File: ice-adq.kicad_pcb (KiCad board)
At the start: 4 copper layers, 86 x 84 mm, 48 parts, among them J1 T_Admisión, J2 T_Escape, J3 T_Aceite, J4 Sonda Lambda, J5 Sens. Inductivo, J6 Sens. Presión, J7 BATT, U1 MAX31855, U2 MAX31855, U3 MAX31855, U4 LM9044, U5 LM358, U6 MAX9924, U7 LM358, U8 hm10, U9 L7805

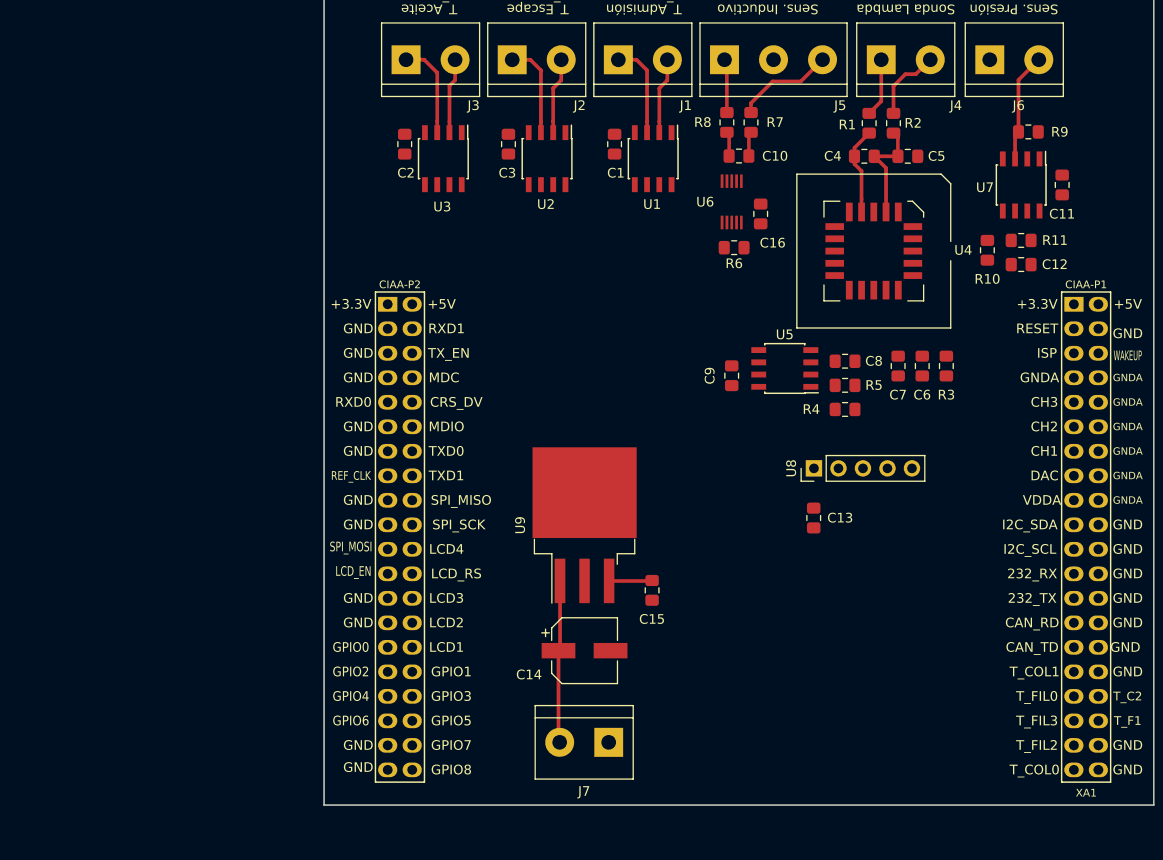
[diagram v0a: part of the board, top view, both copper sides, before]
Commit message: Se cambio pack de 7805 y de 9044
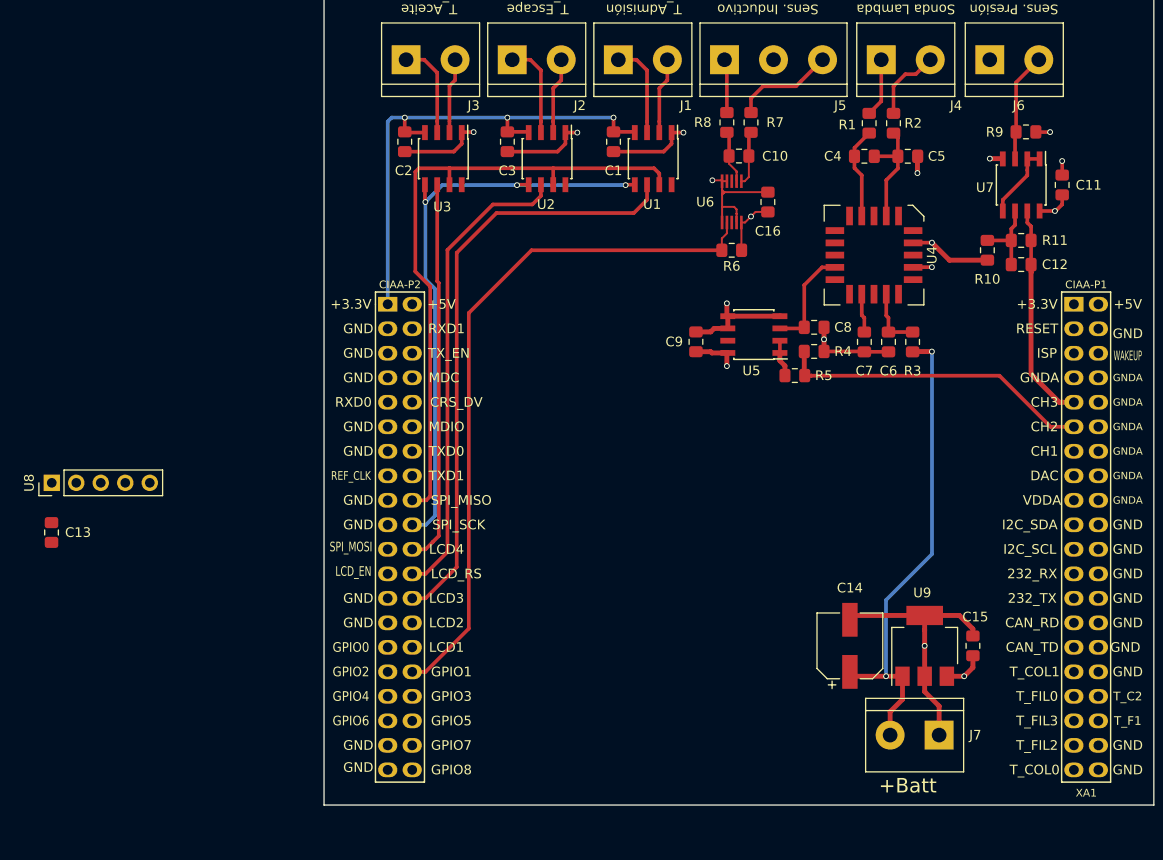
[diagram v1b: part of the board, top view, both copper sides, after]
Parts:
- U4: footprint Package_LCC:PLCC-20_SMD-Socket -> Package_LCC:PLCC-20
- U9: footprint Package_TO_SOT_SMD:TO-263-3_TabPin4 -> Package_TO_SOT_SMD:SOT-223
- moved C13 79.0 mm to (-135.2, 122.8)
- moved U8 79.0 mm to (-135.2, 117.6)
- moved U9 37.4 mm to (-44.8, 134.5)
- moved J7 34.3 mm to (-43.2, 143.8)
- moved C15 33.7 mm to (-39.8, 134.5), turned to 90 degrees
- moved C14 27.5 mm to (-52.5, 134.5), turned to 90 degrees
- moved R4 6.81 mm to (-56.2, 104.0), turned to 180 degrees
- moved R5 5.30 mm to (-58.2, 106.5)
- moved C9 5.11 mm to (-68.5, 103.0)
- moved C8 4.76 mm to (-56.2, 101.5)
- moved U5 4.76 mm to (-62.5, 102.2)
- moved C6 4.30 mm to (-48.5, 103.0)
- moved C7 4.30 mm to (-51.0, 103.0)
- moved R3 4.30 mm to (-46.0, 103.0)
- moved C16 1.44 mm to (-61.0, 88.5)
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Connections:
- C1 pad 1: Net-(C1-Pad1) -> GND
- C1 pad 2: Net-(C1-Pad2) -> +3V3
- C3 pad 1: Net-(C1-Pad1) -> GND
- C3 pad 2: Net-(C1-Pad2) -> +3V3
- U9 pad 4: GND -> (no net)
- XA1 pad 1: +3V3 -> Net-(XA1-Pad1)
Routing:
- net GND: track 0.00 -> 101.2 mm, vias 0 -> 11
- net /rpm/RPM_PULSE: track 0.00 -> 72.4 mm
- net /edu-ciaa/SO: track 0.00 -> 66.5 mm
- net /edu-ciaa/ADM_CS: track 0.00 -> 62.3 mm
- net /edu-ciaa/SCK: track 0.00 -> 61.2 mm, vias 0 -> 3
- net +3V3: track 0.00 -> 53.5 mm, vias 0 -> 3
- net /edu-ciaa/ESC_CS: track 0.00 -> 49.1 mm
- net /edu-ciaa/ACT_CS: track 0.00 -> 39.8 mm
- net +12V: track 16.8 -> 49.9 mm, vias 0 -> 2
- net /edu-ciaa/O2_IN: track 0.00 -> 32.6 mm
- net /edu-ciaa/PRES_IN: track 0.00 -> 22.7 mm
- net +5V: track 4.48 -> 22.2 mm, vias 0 -> 6
- net Net-(C8-Pad1): track 0.00 -> 10.9 mm
- net Net-(C12-Pad1): track 0.00 -> 8.19 mm
- net Net-(U7-Pad1): track 0.00 -> 7.72 mm
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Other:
- net class small added: clearance 0.2032, trace_width 0.2032, via_dia 0.6, via_drill 0.4
- board text added: "+Batt"

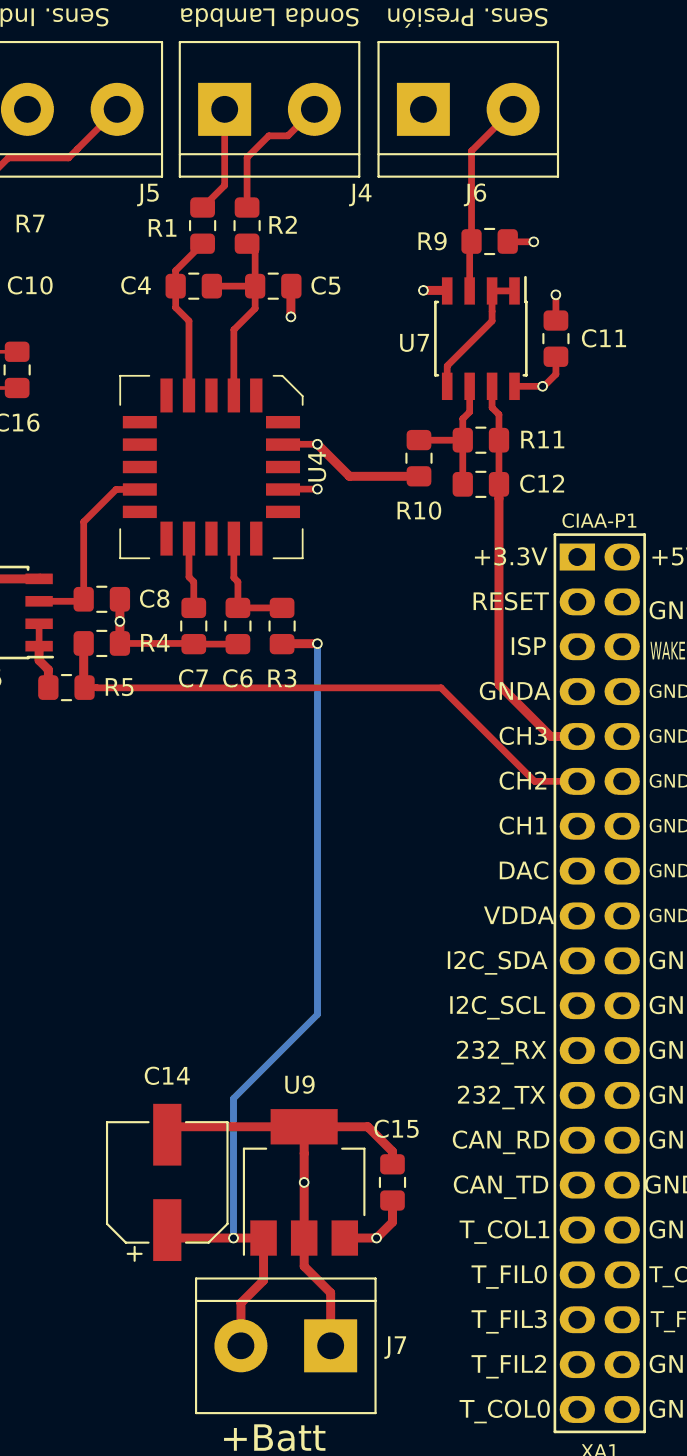
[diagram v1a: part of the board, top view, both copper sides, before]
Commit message: Ruteado de circuito de medicion de bateria
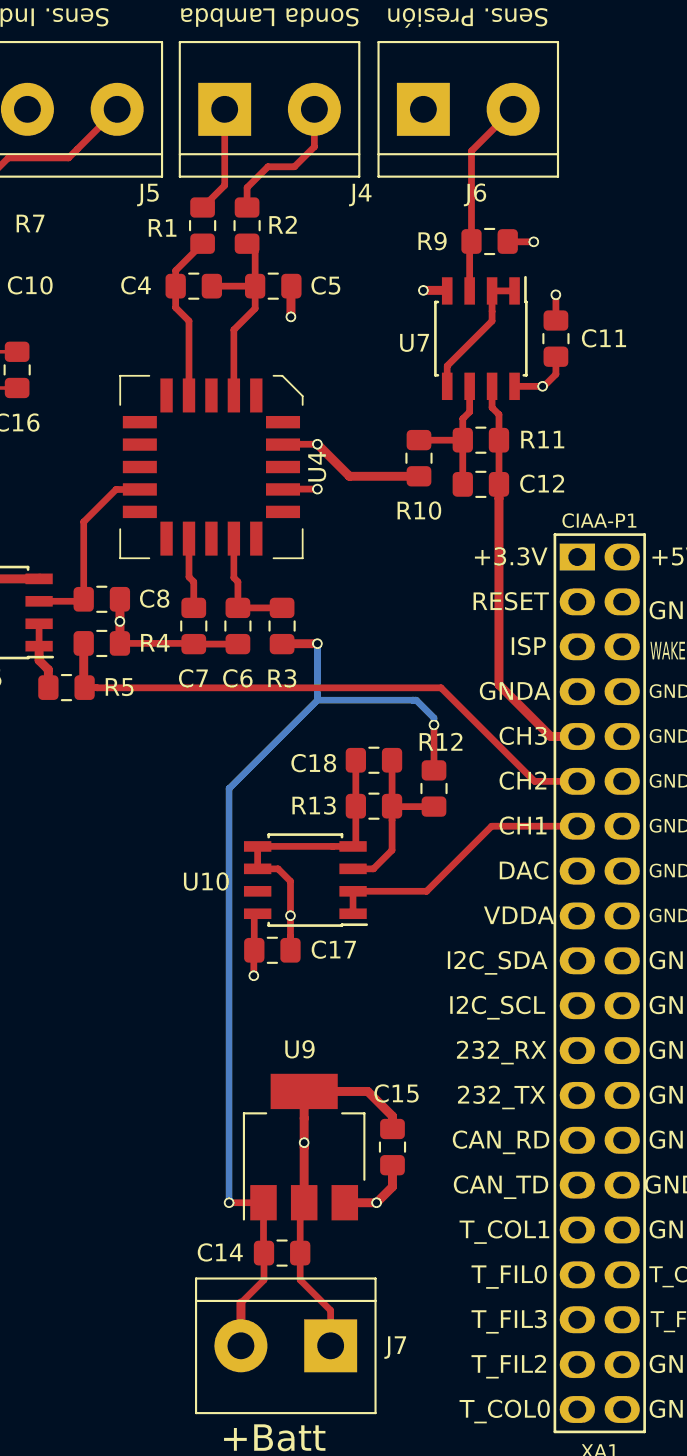
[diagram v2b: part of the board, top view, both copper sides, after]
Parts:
- added C17: 0.01uF, Capacitor_SMD:C_0805_2012Metric_Pad1.15x1.40mm_HandSolder, F.Cu at (-46.5, 121.4)
- added C18: 0.01uF, Capacitor_SMD:C_0805_2012Metric_Pad1.15x1.40mm_HandSolder, F.Cu at (-40.8, 110.6)
- added R12: 39k, Resistor_SMD:R_0805_2012Metric_Pad1.15x1.40mm_HandSolder, F.Cu at (-37.4, 112.2)
- added R13: 10k, Resistor_SMD:R_0805_2012Metric_Pad1.15x1.40mm_HandSolder, F.Cu at (-40.8, 113.2)
- added U10: LM358, Package_SO:SOIC-8_3.9x4.9mm_P1.27mm, F.Cu at (-44.7, 117.4)
- C14: footprint Capacitor_SMD:CP_Elec_6.3x3 -> Capacitor_SMD:C_0805_2012Metric_Pad1.15x1.40mm_HandSolder
- moved C14 7.63 mm to (-46.0, 138.5), turned to 0 degrees
- moved C15 2.00 mm to (-39.8, 132.5)
- moved U9 2.00 mm to (-44.8, 132.5)
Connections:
- XA1 pad 13: Net-(XA1-Pad13) -> /edu-ciaa/V_BATT_IN
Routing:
- net /edu-ciaa/V_BATT_IN: track 0.00 -> 15.6 mm
- net GND: track 101.2 -> 113.1 mm, vias 11 -> 12
- net Net-(C18-Pad1): track 0.00 -> 10.1 mm
- net +12V: track 49.9 -> 56.3 mm, vias 2 -> 3
- net +5V: track 22.2 -> 25.8 mm, vias 6 -> 7

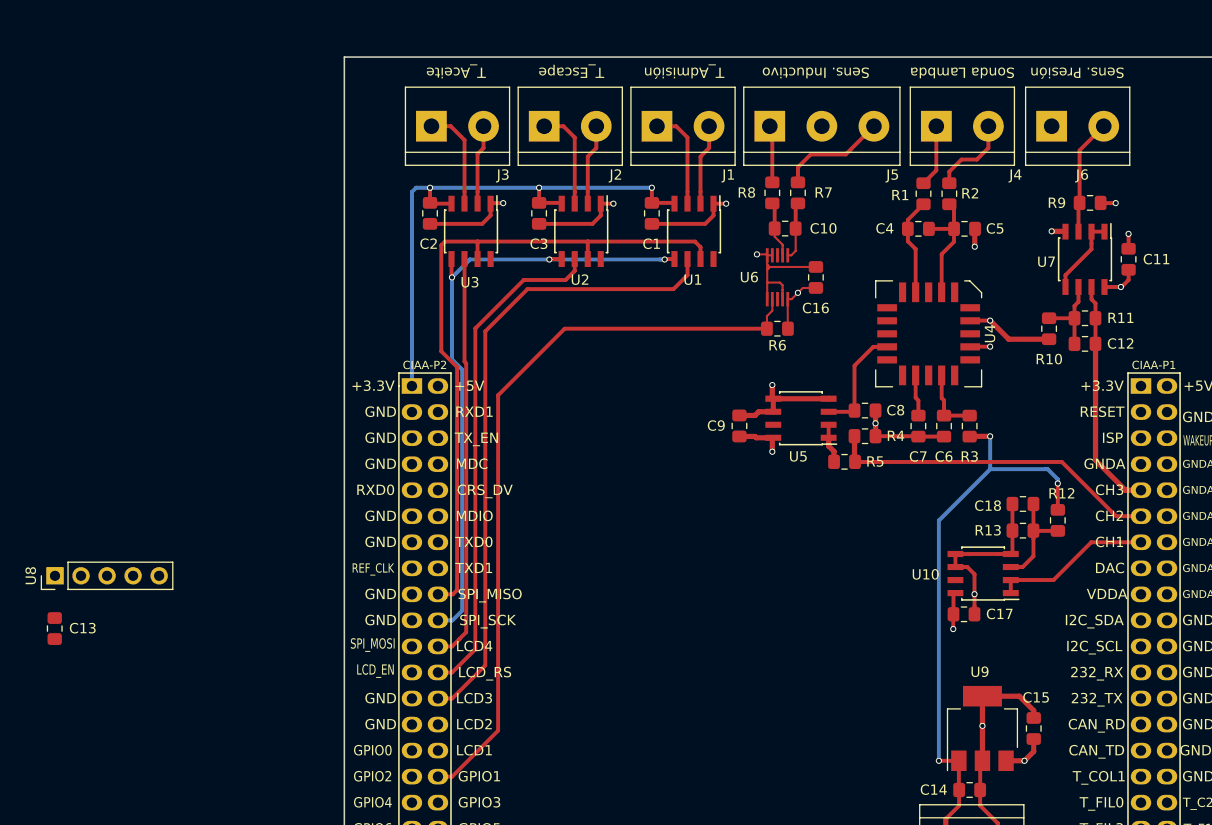
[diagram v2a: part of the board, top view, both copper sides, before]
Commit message: Se agregaron modelos 3d faltantes
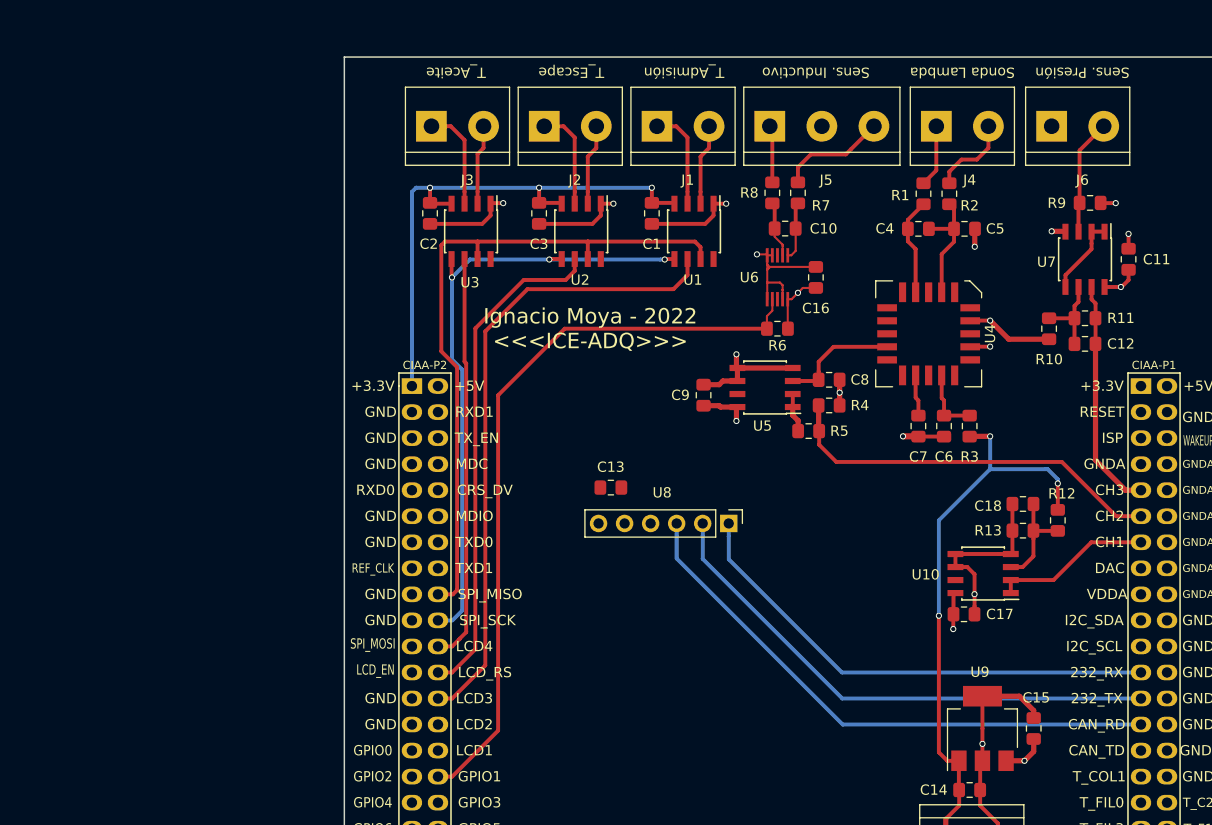
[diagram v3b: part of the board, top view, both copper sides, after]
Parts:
- U8: footprint Connector_PinHeader_2.54mm:PinHeader_1x05_P2.54mm_Vertical -> Connector_PinHeader_2.54mm:PinHeader_1x06_P2.54mm_Vertical
- moved U8 65.9 mm to (-69.5, 112.5), turned to 270 degrees
- moved C13 56.0 mm to (-81.0, 109.0), turned to 0 degrees
- moved C8 4.61 mm to (-59.7, 98.5)
- moved C9 4.61 mm to (-72.0, 100.0)
- moved R4 4.61 mm to (-59.7, 101.0)
- moved R5 4.61 mm to (-61.7, 103.5)
- moved U5 4.61 mm to (-66.0, 99.2)
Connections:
- U9 pad 4: (no net) -> GND
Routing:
- net /comunicaciones/BT_STATE: track 0.00 -> 55.7 mm
- net /comunicaciones/BT_RX: track 0.00 -> 52.1 mm
- net /comunicaciones/BT_TX: track 0.00 -> 48.5 mm
- net /edu-ciaa/O2_IN: track 32.6 -> 38.1 mm
- net GND: track 113.1 -> 110.5 mm, vias 12 -> 13
- net Net-(C8-Pad1): track 10.9 -> 11.6 mm
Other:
- board text added: "Ignacio Moya - 2022 <<<ICE-ADQ>>>"

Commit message: Comitee cambios que estaban hechos.
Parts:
- removed the G*** at (116.4, 96.8)
- removed G101: Logo_OSHWA, footprint:Logo_OSHWA
- removed MP?: Plantilla_EDU-CIAA, footprint:Plantilla_EDU-CIAA
- U8: value hm10 -> hm-10-module
- U9: footprint Package_TO_SOT_SMD:SOT-223 -> Package_TO_SOT_SMD:TO-263-3_TabPin2
- moved C13 184.3 mm to (98.2, 151.8), turned to 180 degrees
- moved C14 178.3 mm to (129.2, 171.2), turned to 90 degrees
- moved U8 176.8 mm to (102.0, 155.5)
- moved C1 175.4 mm to (94.0, 121.2)
- moved C10 175.4 mm to (107.0, 122.7)
- moved C11 175.4 mm to (140.5, 125.7)
- moved C12 175.4 mm to (136.3, 134.0)
- moved C16 175.4 mm to (110.0, 127.5)
- moved C2 175.4 mm to (72.4, 121.2)
- moved C3 175.4 mm to (83.0, 121.2)
- moved C4 175.4 mm to (120.0, 122.8)
- moved C5 175.4 mm to (124.5, 122.8)
- moved C6 175.4 mm to (122.5, 142.0)
- moved C7 175.4 mm to (120.0, 142.0)
- moved C8 175.4 mm to (111.3, 137.5)
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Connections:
- J7 pad 1: GND -> +12V
- J7 pad 2: +12V -> GND
- U8 pad 1: /comunicaciones/BT_TX -> /comunicaciones/BT_STATE
- U8 pad 2: /comunicaciones/BT_RX -> +3V3
- U8 pad 3: /comunicaciones/BT_STATE -> GND
- U8 pad 4: (no net) -> /comunicaciones/BT_TX
- U8 pad 5: (no net) -> /comunicaciones/BT_RX
- U8 pad 6: (no net) -> Net-(U8-Pad6)
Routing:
- net +3V3: track 53.5 -> 92.4 mm, vias 3 -> 4
- net GND: track 110.5 -> 142.1 mm, vias 13 -> 16
- net /comunicaciones/BT_TX: track 48.5 -> 52.7 mm
- net /comunicaciones/BT_RX: track 52.1 -> 56.2 mm
- net /comunicaciones/BT_STATE: track 55.7 -> 51.9 mm, vias 0 -> 1
- net +5V: track 25.8 -> 29.4 mm, vias 7 -> 9
- net Net-(C18-Pad1): track 10.1 -> 12.9 mm
- net /edu-ciaa/V_BATT_IN: track 15.6 -> 14.3 mm
- net +12V: track 55.8 -> 56.2 mm, vias 3 -> 2
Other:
- net class Default removed
- net class small removed
- rule pad_to_mask_clearance: 0.2 -> 0
- board text added: "(-)Batt(+)"
- board text added: "PROTOTIPO NO APTO PARA VENTA"
- board text removed: "+Batt"
- board text removed: "Borrar (Footprint MP1) la Plantilla-EDU-CIAA al finalizar el posicionamiento y definido el borde de PCB."
- board text removed: "Diseño simple faz. Sin requerimientos especiales."
- board text removed: "Editar el rótulo"
- board text removed: "Editar este cuadro para reflejar cantidad de capas, si se han realizado cálculos de impedancia o si es relevante para el funcionamiento."
- board text removed: "PONCHO BASICO http://www.proyecto-ciaa.com.ar/"
- board text removed: "STACK-UP"
- board text removed: "Se sugiere colocar Nombre de Poncho y autor en cobre, serigrafía y rótulo."
